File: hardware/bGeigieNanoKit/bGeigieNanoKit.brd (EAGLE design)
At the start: 96.2 x 66.7 mm, 37 parts, among them T1 2SC1815

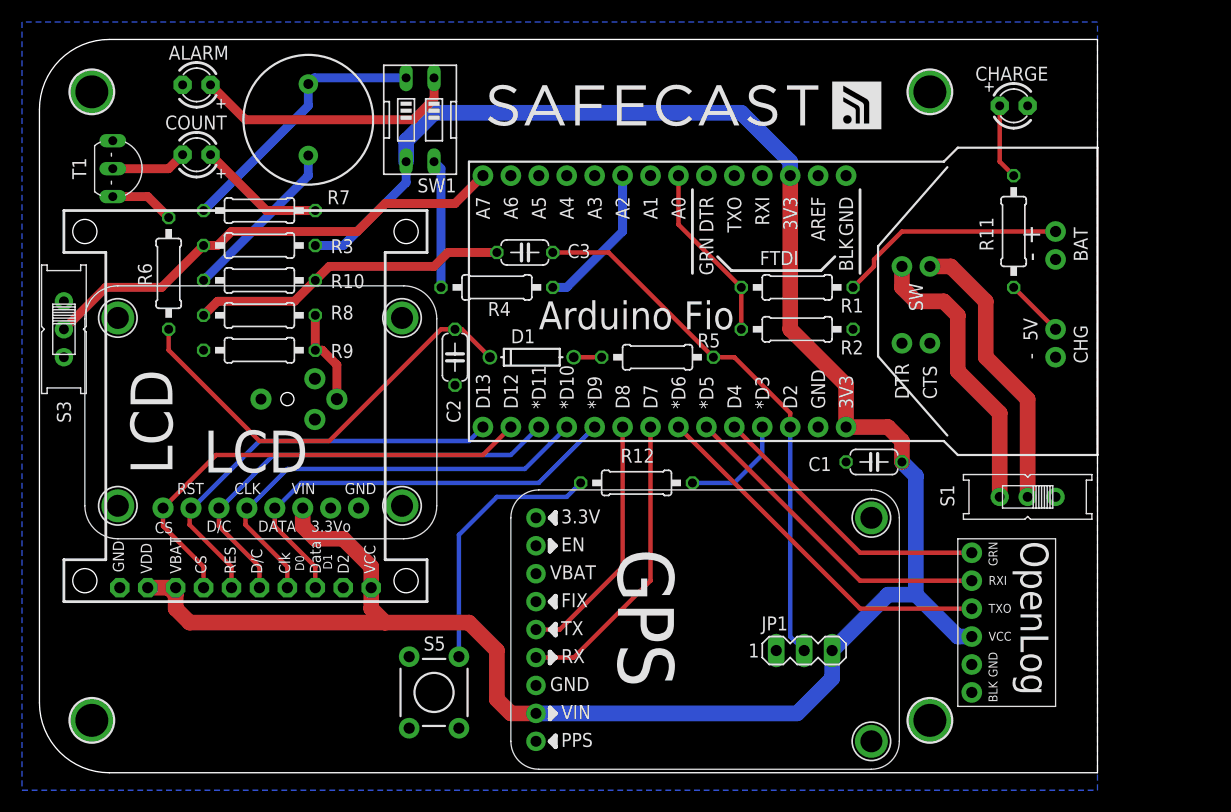
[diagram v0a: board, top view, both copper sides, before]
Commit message: gererating outputs for single OLED layout. changigng to toggle switch
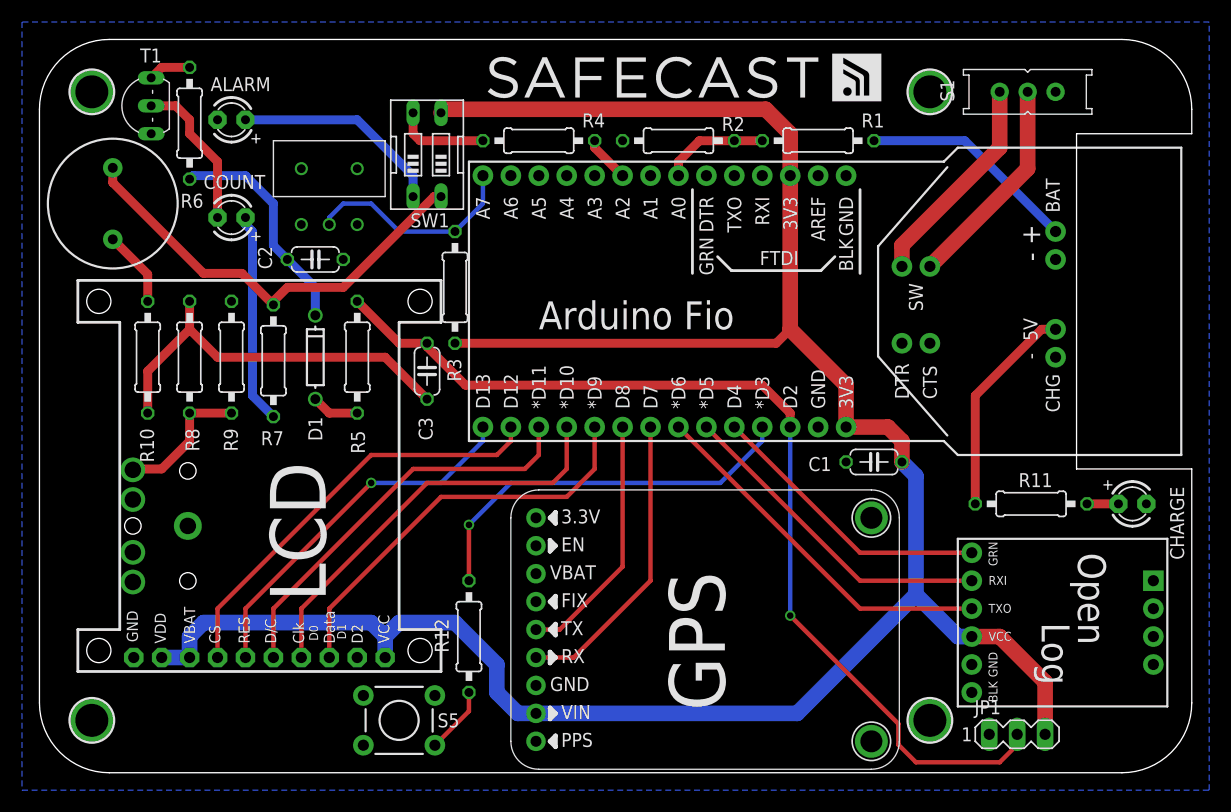
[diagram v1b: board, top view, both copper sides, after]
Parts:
- removed S3: (no value), adafruit:EG1218
- removed U1: (no value), SparkFun:STEREOJACK2.5MM_STEREOJACK2.5MM
- added CN1: (no value), microbuilder:STX3100
- U$1: value OPENLOG_MINITOP -> OPENLOG; device open_hw_sockets:OPENLOG_TOP_MINI -> open_hw_sockets:OPENLOG
- U$4: value LCD -> A12JH; device open_hw_sockets:SSD1306_128X32_SPI_LCD_TOP -> open_hw_sockets:A12AH
- U$5: value SSD1306_128X64_LCD_MIN -> LCD
- moved U$4 40.3 mm to (27.9, 56.5), turned to 180 degrees
- moved CHARGE 37.8 mm to (101.0, 26.0)
- moved S1 36.8 mm to (91.4, 63.5)
- moved R5 27.3 mm to (30.5, 39.4), turned to 270 degrees
- moved R11 24.8 mm to (91.8, 26.0), turned to 180 degrees
- moved JP1 20.8 mm to (90.5, 5.08)
- moved R12 20.7 mm to (40.6, 14.0), turned to 90 degrees
- moved R2 20.3 mm to (59.7, 59.1), turned to 0 degrees
- moved D1 19.7 mm to (26.7, 39.4), turned to 90 degrees
- moved SG1 19.3 mm to (8.26, 53.3)
- moved R3 18.2 mm to (39.4, 45.7), turned to 270 degrees
- moved C2 15.5 mm to (26.7, 48.3), turned to 0 degrees
- moved C3 14.0 mm to (36.8, 38.1), turned to 90 degrees
- moved R4 13.9 mm to (47.0, 59.1)
- moved R6 13.8 mm to (15.2, 60.6)
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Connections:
- net GND: now also CN1.1, U$4.P$3, U$4.P$4, U$4.P$5; no longer S3.S, U$4.JP1$8, U$4.U$2$P$1, U$4.U$3$P$1, U$4.U$4$P$1, U$4.U$5$P$1, U1.RING1, U1.RING2
- net N$1: no longer U$4.JP1$5
- net N$14: now also U$4.P$2; no longer S3.P
- net N$2: no longer U$4.JP1$4
- net N$25: now also CN1.2; no longer U1.TIP
- net N$3: no longer U$4.JP1$3
- net N$4: no longer U$4.JP1$1
- net N$5: no longer U$4.JP1$2
- net VCC: no longer U$4.JP1$6
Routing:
- net N$18: track 49.8 -> 91.1 mm, vias 0 -> 1
- net N$30: track 9.94 -> 36.2 mm, vias 0 -> 1
- net N$14: track 43.9 -> 19.8 mm
- net N$27: track 39.8 -> 20.5 mm
- net N$20: track 24.1 -> 6.08 mm
- net N$21: track 24.6 -> 40.1 mm
- net VIN: track 5.39 -> 19.6 mm
- net VCC: track 204.8 -> 215.8 mm
- net N$15: track 13.5 -> 4.23 mm
- net N$23: track 15.3 -> 6.96 mm
- net N$19: track 11.6 -> 19.1 mm
- net N$22: track 6.88 -> 14.0 mm
- net N$24: track 29.0 -> 36.0 mm
- net N$11: track 16.3 -> 9.68 mm
- net N$13: track 26.1 -> 19.6 mm
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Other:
- board size 96.2 x 66.7 mm -> 104.8 x 66.7 mm

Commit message: Changed R5 and R9 to 4.7 k
For decreasing the load on the IRover output to prevent lower CPM count.
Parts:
- R5, R9: value 1k -> 4.7k
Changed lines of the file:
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@@
 <?xml version="1.0" encoding="utf-8"?>
 <!DOCTYPE eagle SYSTEM "eagle.dtd">
-<eagle version="6.3">
+<eagle version="6.4">
 <drawing>
 <settings>
@@
 <attribute name="VALUE" x="45.9994" y="58.42" size="1.27" layer="27" ratio="10"/>
 </element>
-<element name="R5" library="rcl" package="0207/10" value="1k" x="30.48" y="39.37" smashed="yes" rot="R270">
+<element name="R5" library="rcl" package="0207/10" value="4.7k" x="30.48" y="39.37" smashed="yes" rot="R270">
 <attribute name="NAME" x="31.1785" y="30.607" size="1.27" layer="25" ratio="10" rot="R90"/>
 <attribute name="VALUE" x="31.115" y="38.3794" size="1.27" layer="27" ratio="10" rot="R90"/>
@@
 <attribute name="VALUE" x="14.605" y="40.6781" size="1.27" layer="27" ratio="10" rot="R270"/>
 </element>
-<element name="R9" library="rcl" package="0207/10" value="1k" x="19.05" y="39.37" smashed="yes" rot="R90">
+<element name="R9" library="rcl" package="0207/10" value="4.7k" x="19.05" y="39.37" smashed="yes" rot="R90">
 <attribute name="NAME" x="18.3515" y="32.893" size="1.27" layer="25" ratio="10" rot="R270"/>
 <attribute name="VALUE" x="18.415" y="40.3606" size="1.27" layer="27" ratio="10" rot="R270"/>
